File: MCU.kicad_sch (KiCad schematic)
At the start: 8 parts

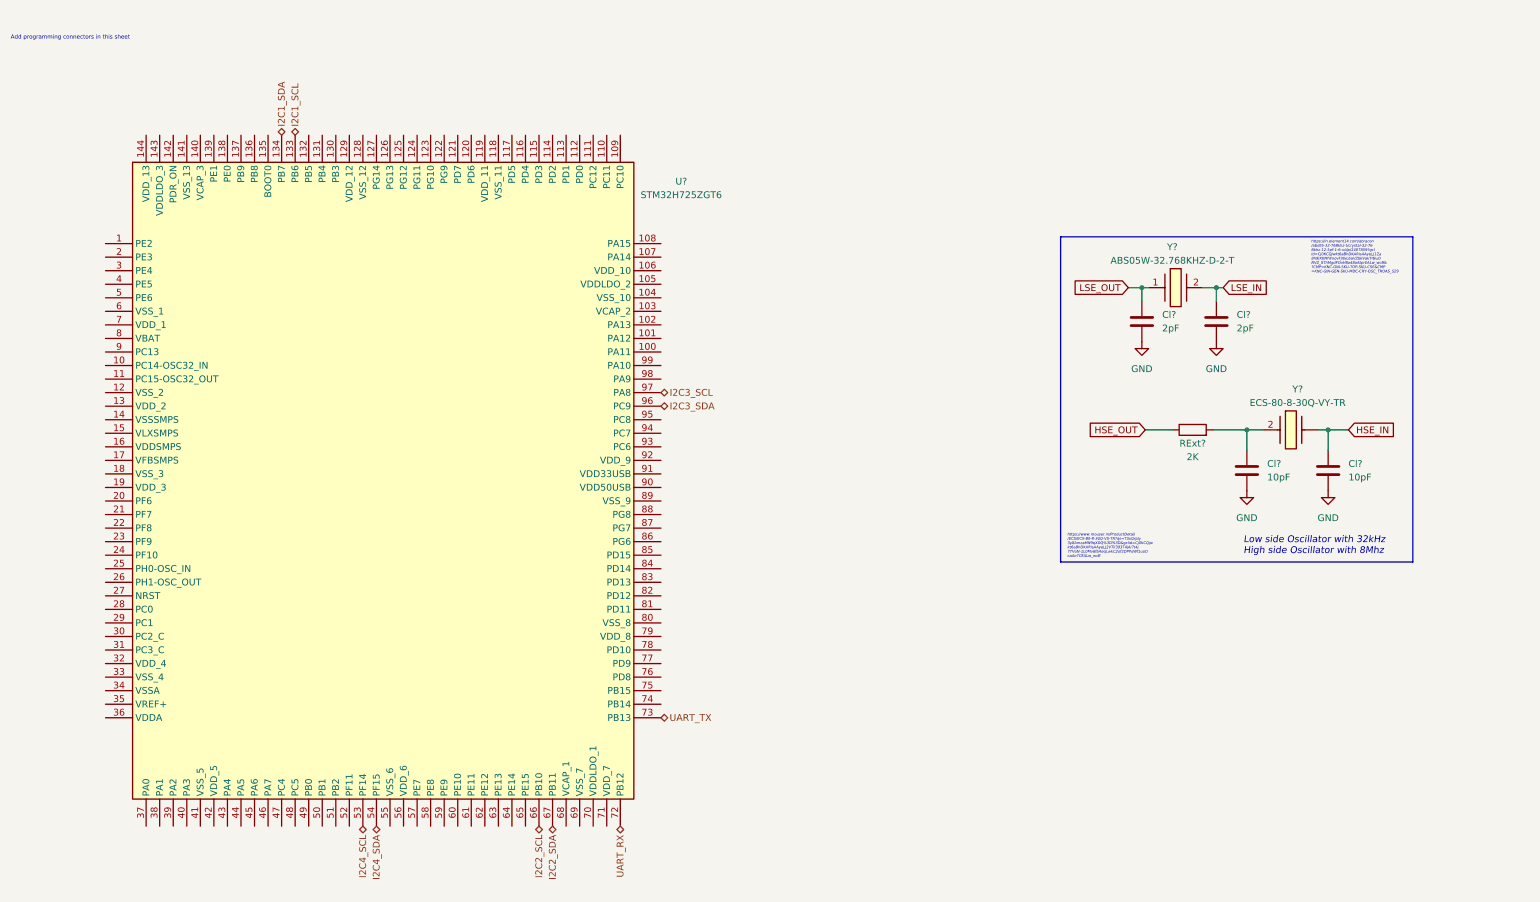
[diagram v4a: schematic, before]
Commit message: JTAG 10 pin and 20 pin are added. Please make a decision
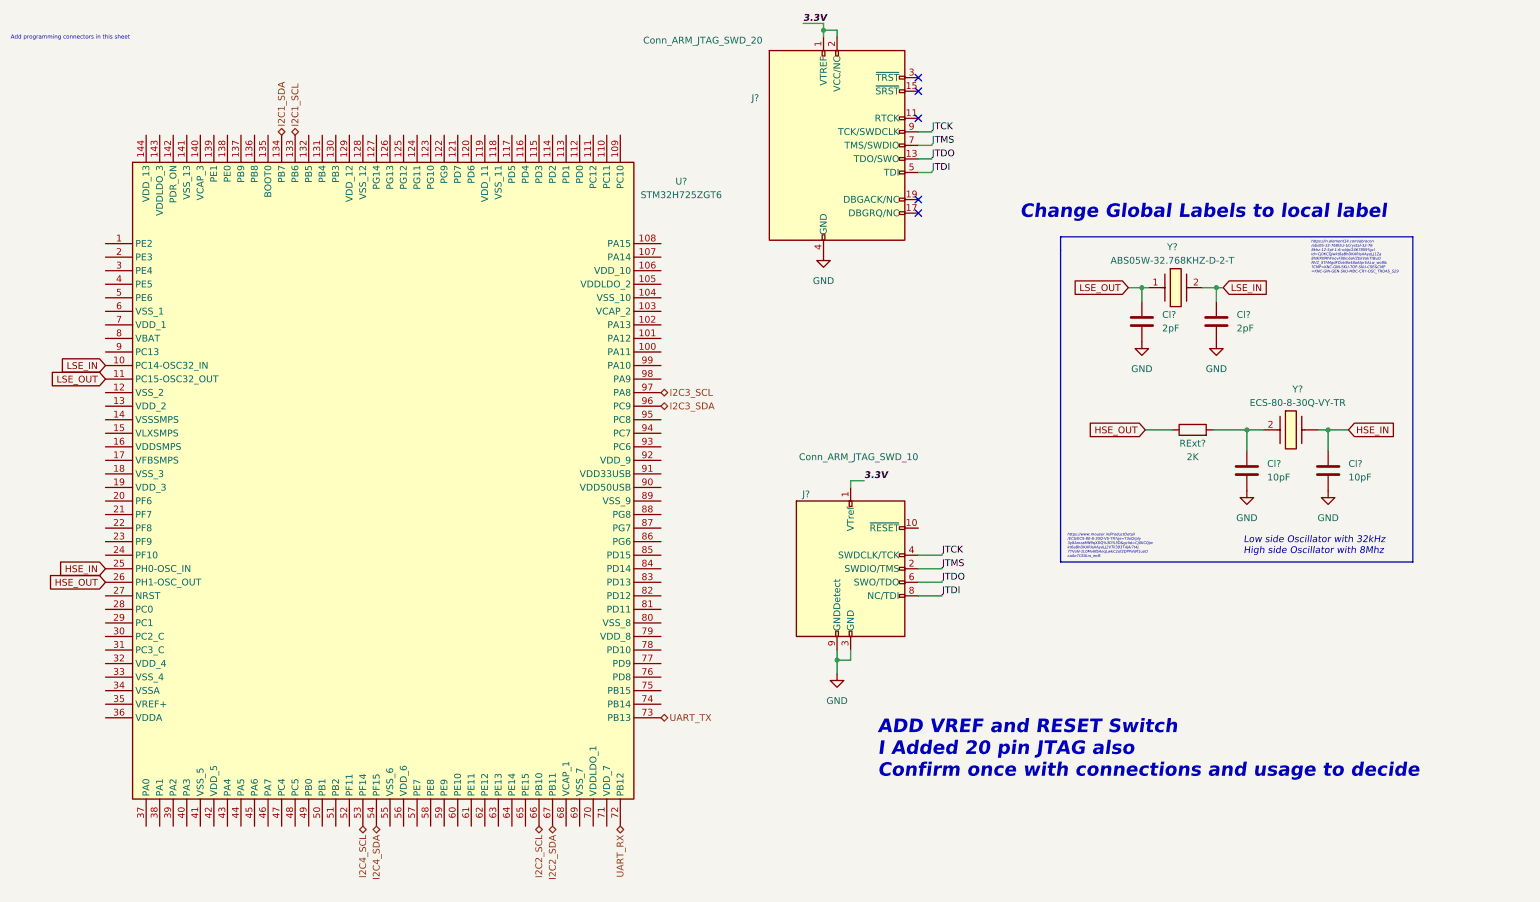
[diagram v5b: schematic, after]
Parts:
- added J?: Conn_ARM_JTAG_SWD_10, symbol Connector:Conn_ARM_JTAG_SWD_10
- added J?: Conn_ARM_JTAG_SWD_20, symbol Connector:Conn_ARM_JTAG_SWD_20
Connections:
- net GND: now also J?.10 (GND), J?.12 (GND), J?.14 (GND), J?.16 (GND), J?.18 (GND), J?.20 (GND), J?.3 (GND), J?.4 (GND), J?.5 (GND), J?.6 (GND), J?.8 (GND), J?.9 (GNDDetect)
- net HSE_IN: now also U?.25 (PH0-OSC_IN)
- net HSE_OUT: now also U?.26 (PH1-OSC_OUT)
- net LSE_IN: now also U?.10 (PC14-OSC32_IN)
- net LSE_OUT: now also U?.11 (PC15-OSC32_OUT)
- new net 3.3V: J?.1 (VTREF), J?.1 (VTref), J?.2 (VCC/NC)
- new net JTCK: J?.4 (SWDCLK/TCK), J?.9 (TCK/SWDCLK)
- new net JTDI: J?.5 (TDI), J?.8 (NC/TDI)
- new net JTDO: J?.13 (TDO/SWO), J?.6 (SWO/TDO)
- new net JTMS: J?.2 (SWDIO/TMS), J?.7 (TMS/SWDIO)
- no-connect marks 0 -> 5
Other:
- note added: "ADD VREF and RESET Switch I Added 20 pin JTAG also Confirm once with connections and usage to decide"
- note added: "Change Global Labels to local label"

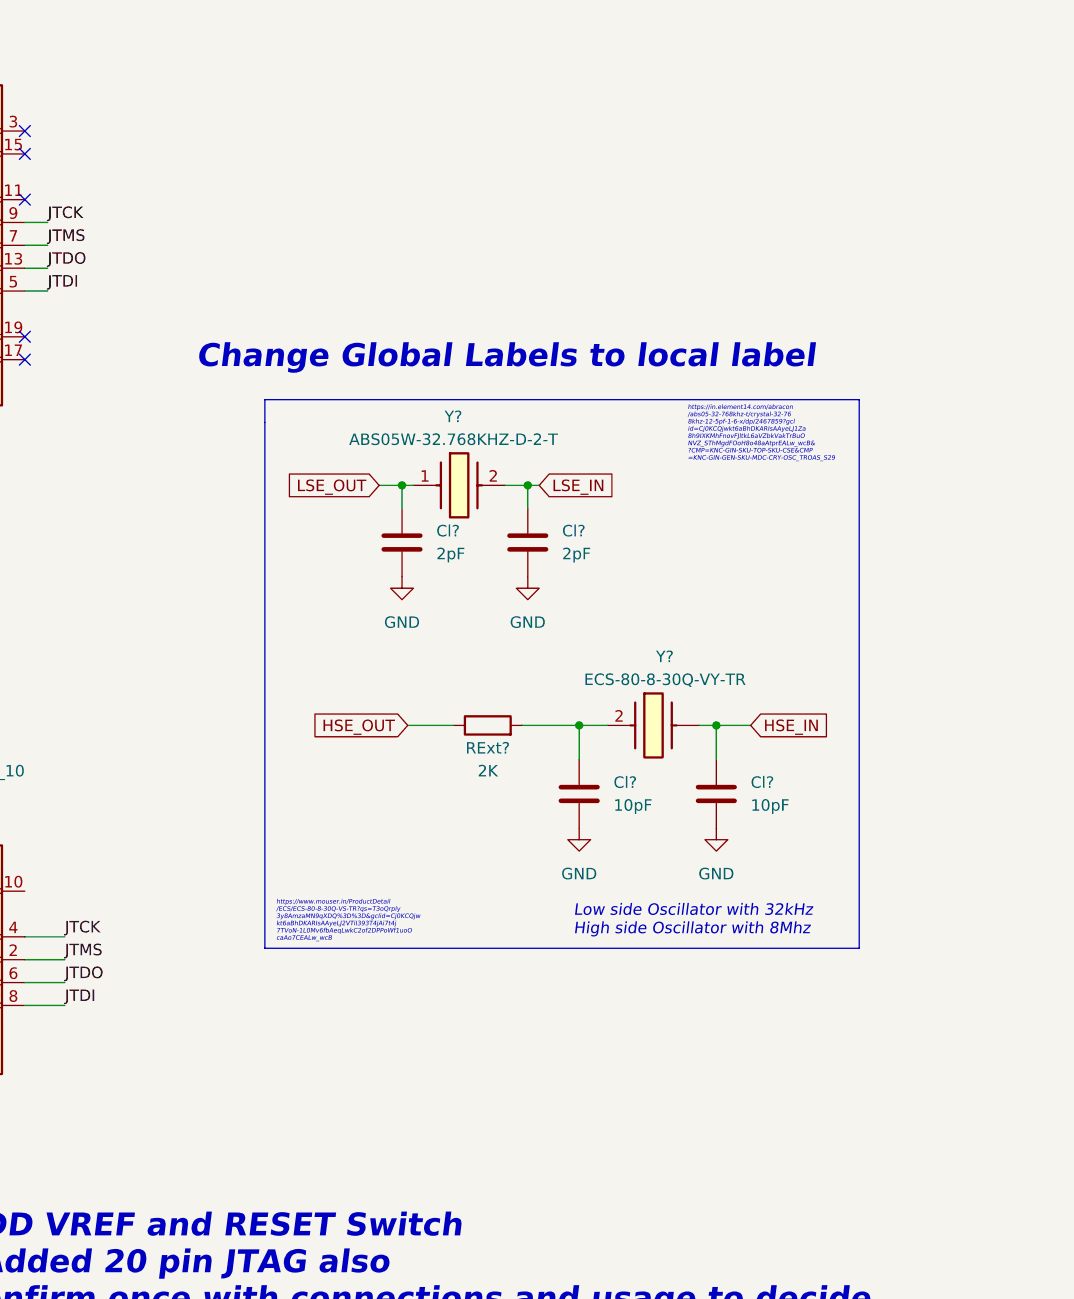
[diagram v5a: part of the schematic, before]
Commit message: EEPROM 32 Mbit added
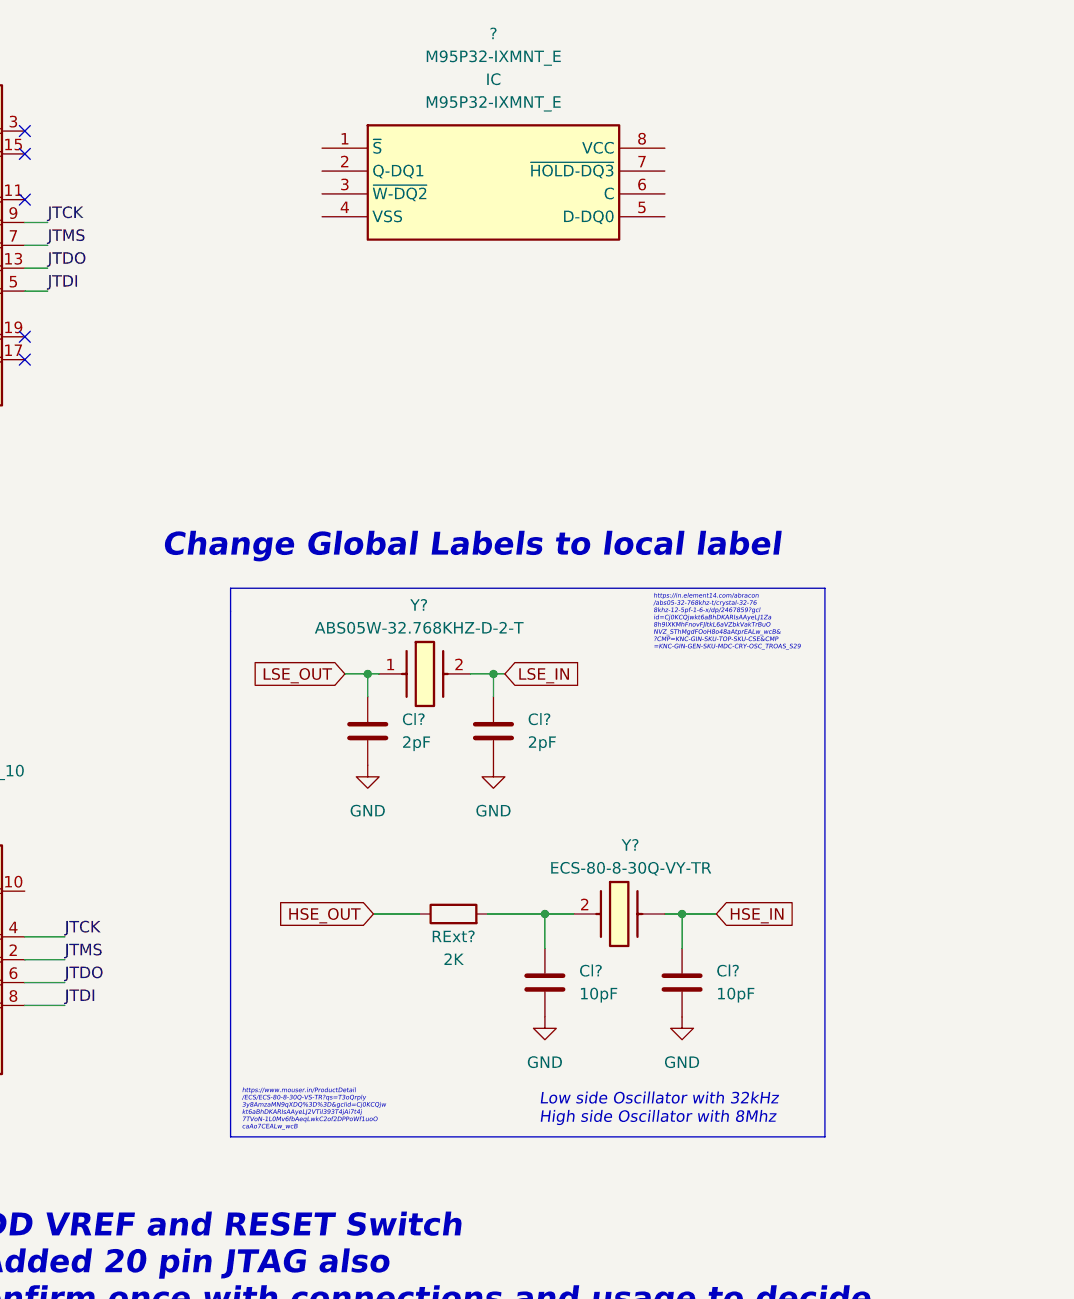
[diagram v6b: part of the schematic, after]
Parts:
- added ?: M95P32-IXMNT_E, symbol M95P32-IXMNT_E:M95P32-IXMNT_E
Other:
- moved on the sheet: Cl?, RExt?, Y?

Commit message: eeprom fanned out
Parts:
- gave numbers to parts that had none: 6
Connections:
- net GND: now also U2.4 (VSS)
- net CS: now reaches U2.1 (~{S})
- net MISO: now reaches U2.2 (Q-DQ1)
- net WP_bar: now reaches U2.3 (~{W-DQ2})
- net MOSI: now reaches U2.5 (D-DQ0)
- net SPI_SCK: now reaches U2.6 (C)
- net HOLD_bar: now reaches U2.7 (~{HOLD-DQ3})
- net MCU_POW: now reaches U2.8 (VCC)
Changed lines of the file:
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@@
+    (stroke (width 0) (type default) (color 0 0 0 0))
+  )
+  (wire (pts (xy 259.08 33.02) (xy 264.16 33.02))
     (stroke (width 0) (type default) (color 0 0 0 0))
   )
@@
     (stroke (width 0) (type default) (color 0 0 0 0))
   )
+  (wire (pts (xy 217.17 27.94) (xy 220.98 27.94))
+    (stroke (width 0) (type default) (color 0 0 0 0))
+  )
   (wire (pts (xy 226.06 86.36) (xy 226.06 88.9))
     (stroke (width 0) (type default) (color 0 0 0 0))
@@
     (stroke (width 0) (type default) (color 0 0 0 0))
   )
+  (wire (pts (xy 218.44 35.56) (xy 218.44 36.83))
+    (stroke (width 0) (type default) (color 0 0 0 0))
+  )
   (wire (pts (xy 172.72 135.255) (xy 172.72 137.795))
     (stroke (width 0) (type default) (color 0 0 0 0))
@@
     (stroke (width 0) (type default) (color 0 0 0 0))
   )
+  (wire (pts (xy 217.17 30.48) (xy 220.98 30.48))
+    (stroke (width 0) (type default) (color 0 0 0 0))
+  )
   (wire (pts (xy 260.985 113.03) (xy 260.985 116.84))
     (stroke (width 0) (type default) (color 0 0 0 0))
@@
     (stroke (width 0) (type default) (color 0 0 0 0))
   )
+  (wire (pts (xy 259.08 27.94) (xy 264.16 27.94))
+    (stroke (width 0) (type default) (color 0 0 0 0))
+  )
   (wire (pts (xy 172.72 133.35) (xy 172.72 135.255))
     (stroke (width 0) (type default) (color 0 0 0 0))
@@
     (stroke (width 0) (type default) (color 0 0 0 0))
   )
+  (wire (pts (xy 220.98 35.56) (xy 218.44 35.56))
+    (stroke (width 0) (type default) (color 0 0 0 0))
+  )
   (wire (pts (xy 245.745 113.03) (xy 248.92 113.03))
     (stroke (width 0) (type default) (color 0 0 0 0))
   )
   (wire (pts (xy 170.18 15.875) (xy 170.18 17.145))
+    (stroke (width 0) (type default) (color 0 0 0 0))
+  )
+  (wire (pts (xy 259.08 30.48) (xy 264.16 30.48))
+    (stroke (width 0) (type default) (color 0 0 0 0))
+  )
+  (wire (pts (xy 217.17 33.02) (xy 220.98 33.02))
+    (stroke (width 0) (type default) (color 0 0 0 0))
+  )
+  (wire (pts (xy 259.08 35.56) (xy 264.16 35.56))
     (stroke (width 0) (type default) (color 0 0 0 0))
   )
@@
     (effects (font (size 1.27 1.27)) (justify left bottom))
   )
+  (label "CS" (at 217.17 27.94 180)
+    (effects (font (size 1.27 1.27)) (justify right bottom))
+  )
   (label "JTDO" (at 192.405 120.65 0)
     (effects (font (size 1.27 1.27)) (justify left bottom))
   )
   (label "JTMS" (at 192.405 118.11 0)
+    (effects (font (size 1.27 1.27)) (justify left bottom))
+  )
+  (label "MISO" (at 217.17 30.48 180)
+    (effects (font (size 1.27 1.27)) (justify right bottom))
+  )
+  (label "MOSI" (at 264.16 35.56 0)
+    (effects (font (size 1.27 1.27)) (justify left bottom))
+  )
+  (label "WP_bar" (at 217.17 33.02 180)
+    (effects (font (size 1.27 1.27)) (justify right bottom))
+  )
+  (label "SPI_SCK" (at 264.16 33.02 0)
     (effects (font (size 1.27 1.27)) (justify left bottom))
   )
@@
   (label "3.3V" (at 177.8 101.6 0)
     (effects (font (size 1.27 1.27) bold italic) (justify left bottom))
+  )
+  (label "HOLD_bar" (at 264.16 30.48 0)
+    (effects (font (size 1.27 1.27)) (justify left bottom))
   )
   (global_label "LSE_IN" (shape input) (at 241.3 86.36 0) (fields_autoplaced)
@@
     (effects (font (size 1.27 1.27)) (justify left))
   )
+  (hierarchical_label "MCU_POW" (shape bidirectional) (at 264.16 27.94 0)
+    (effects (font (size 1.27 1.27)) (justify left))
+  )
   (hierarchical_label "I2C1_SCL" (shape bidirectional) (at 71.12 36.83 90)
     (effects (font (size 1.27 1.27)) (justify left))
@@
   (symbol (lib_id "ABS05W-32_768KHZ-D-2-T:ABS05W-32.768KHZ-D-2-T") (at 227.33 86.36 0) (unit 1)
     (in_bom yes) (on_board yes)
-    (property "Reference" "Y?" (id 0) (at 231.775 78.74 0))
+    (property "Reference" "Y1" (id 0) (at 231.775 78.74 0))
     (property "Value" "ABS05W-32.768KHZ-D-2-T" (id 1) (at 231.775 81.28 0))
     (property "Footprint" "ABS05W-32.768KHZ-D-2-T:ABS05W32768KHZD2T" (id 2) (at 227.33 86.36 0)
@@
   (symbol (lib_id "STM32H725ZGT6:STM32H725ZGT6") (at 35.56 57.15 0) (unit 1)
     (in_bom no) (on_board yes) (fields_autoplaced)
-    (property "Reference" "U?" (id 0) (at 143.51 45.4912 0))
-    (property "Value" "STM32H725ZGT6" (id 1) (at 143.51 48.0312 0))
+    (property "Reference" "U1" (id 0) (at 143.51 50.5712 0))
+    (property "Value" "STM32H725ZGT6" (id 1) (at 143.51 53.1112 0))
     (property "Footprint" "STM32H725ZGT6:QFP50P2200X2200X160-144N" (id 2) (at 35.56 57.15 0)
       (effects (font (size 1.27 1.27)) hide)
@@
   (symbol (lib_id "Connector:Conn_ARM_JTAG_SWD_10") (at 175.26 118.11 0) (unit 1)
     (in_bom yes) (on_board yes)
-    (property "Reference" "J?" (id 0) (at 167.64 104.14 0)
+    (property "Reference" "J1" (id 0) (at 167.64 104.14 0)
       (effects (font (size 1.27 1.27)) (justify right))
     )
@@
     (pin "2")
   )
+  (symbol (lib_name "GND_1") (lib_id "power:GND") (at 218.44 36.83 0) (unit 1)
+    (in_bom yes) (on_board yes) (fields_autoplaced)
+    (property "Reference" "#PWR?" (id 0) (at 218.44 43.18 0)
+      (effects (font (size 1.27 1.27)) hide)
+    )
+    (property "Value" "GND" (id 1) (at 218.44 41.91 0))
+    (property "Footprint" "" (id 2) (at 218.44 36.83 0)
+      (effects (font (size 1.27 1.27)) hide)
+    )
+    (property "Datasheet" "" (id 3) (at 218.44 36.83 0)
+      (effects (font (size 1.27 1.27)) hide)
+    )
+    (pin "1")
+  )
   (symbol (lib_id "Connector:Conn_ARM_JTAG_SWD_20") (at 172.72 38.735 0) (unit 1)
     (in_bom yes) (on_board yes)
-    (property "Reference" "J?" (id 0) (at 158.115 29.845 0)
+    (property "Reference" "JTAG" (id 0) (at 158.115 29.845 0)
       (effects (font (size 1.27 1.27)) (justify right))
     )
@@
   (symbol (lib_id "M95P32-IXMNT_E:M95P32-IXMNT_E") (at 220.98 27.94 0) (unit 1)
     (in_bom yes) (on_board yes) (fields_autoplaced)
-    (property "Reference" "?" (id 0) (at 240.03 15.24 0))
+    (property "Reference" "U2" (id 0) (at 240.03 15.24 0))
     (property "Value" "M95P32-IXMNT_E" (id 1) (at 240.03 17.78 0))
     (property "Footprint" "" (id 2) (at 220.98 27.94 0)
@@
   (symbol (lib_id "ECS-80-8-30Q-VY-TR:ECS-80-8-30Q-VY-TR") (at 248.92 113.03 0) (unit 1)
     (in_bom yes) (on_board yes)
-    (property "Reference" "Y?" (id 0) (at 255.27 105.41 0))
+    (property "Reference" "Y2" (id 0) (at 255.27 105.41 0))
     (property "Value" "ECS-80-8-30Q-VY-TR" (id 1) (at 255.27 107.95 0))
     (property "Footprint" "ECS-80-8-30Q-VY-TR:ECS80830QVYTR" (id 2) (at 248.92 113.03 0)
